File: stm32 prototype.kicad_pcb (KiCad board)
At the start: 4 copper layers, 112 parts, among them J1 USB_B_Mini, J2 Conn_01x06, J3 Conn_02x08_Top_Bottom, J4 Conn_01x10, J5 Conn_02x04_Top_Bottom, Q1 Q_NMOS_GSD, Q10 2N2219, Q11 Q_NMOS_GSD, Q2 Q_NMOS_GSD, Q3 Q_NMOS_GSD, Q4 Q_NMOS_GSD, Q5 Q_NMOS_GSD, Q6 Q_NMOS_GSD, Q7 Q_NMOS_GSD, Q8 Q_NMOS_GSD, Q9 2N2219, SW1 SW_Push, SW2 SW_Push, U1 FT232RL, U2 W25Q128JV-DTR, U3 STM32F407VGTx, U4 LD1117S33TR, U5 ESP32-WROOM, U7 TPS62203DBVR, Y1 Crystal_GND24

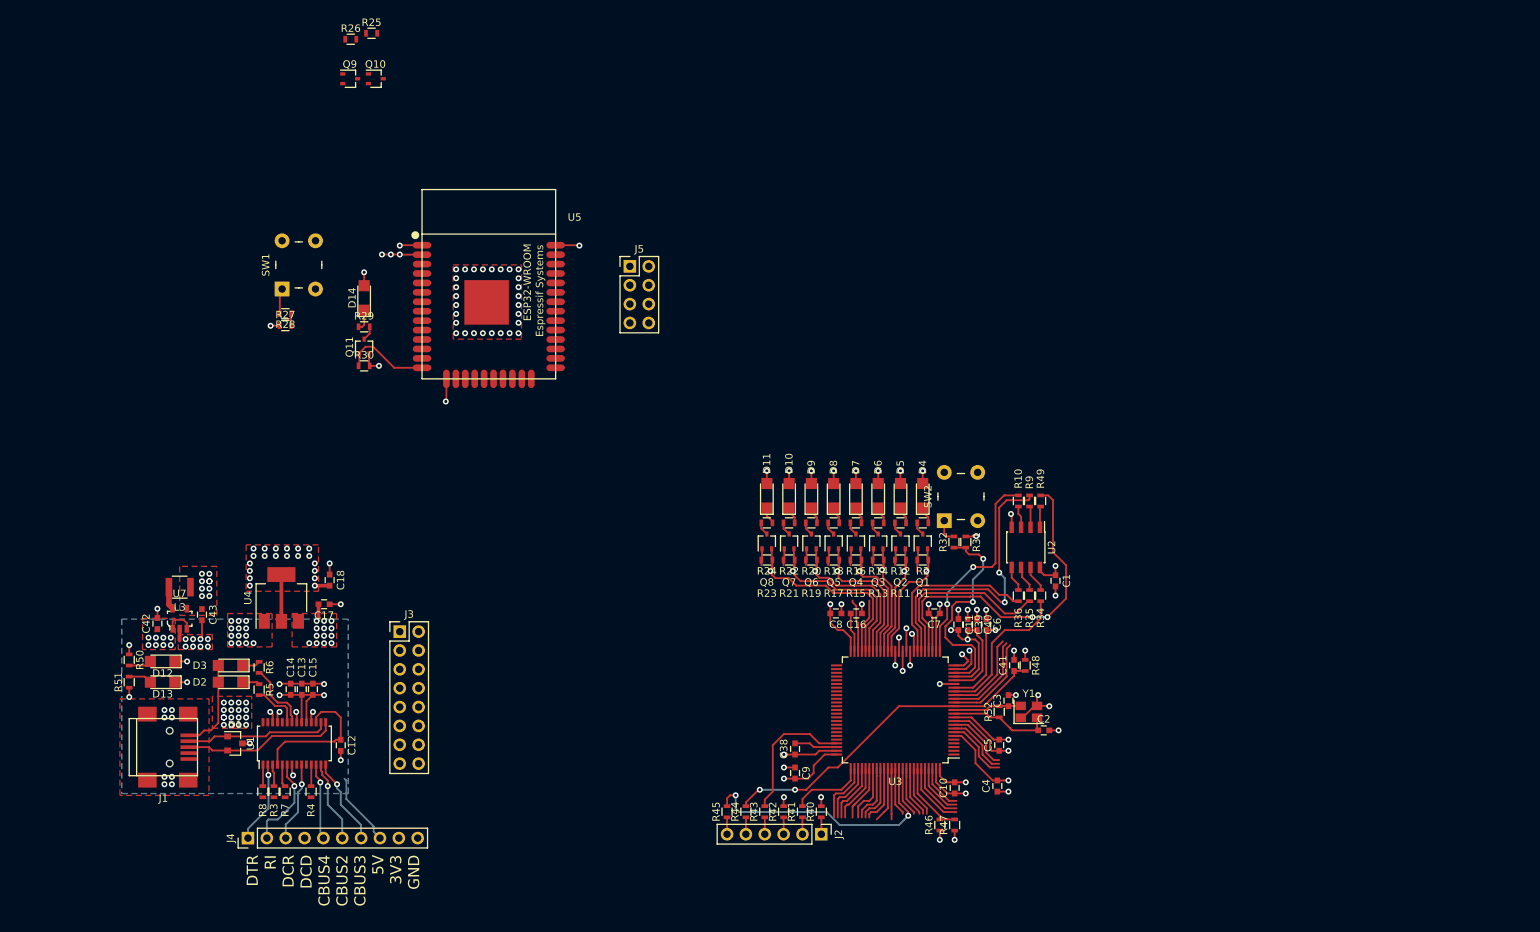
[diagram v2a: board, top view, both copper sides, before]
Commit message: worked on layout, created board outline, started working on fitting the input, esp32, and stm32 sections together
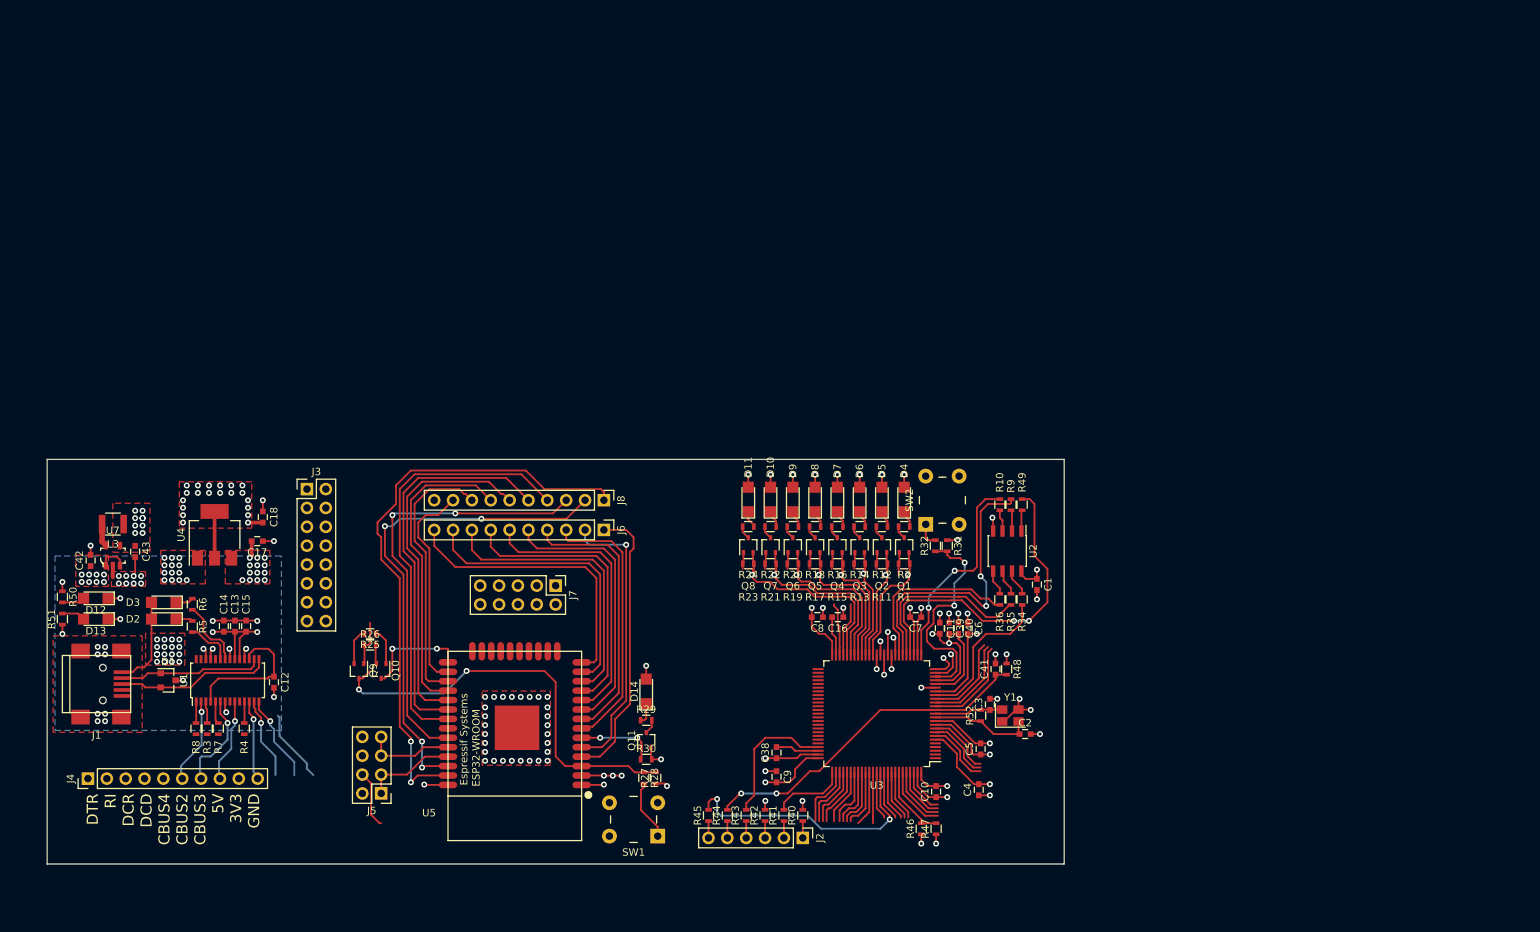
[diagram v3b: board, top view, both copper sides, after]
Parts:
- added J6: Conn_01x10, Pin_Headers:Pin_Header_Straight_1x10_Pitch2.54mm, F.Cu at (137.5, 97.5)
- added J7: Conn_02x05_Top_Bottom, Pin_Headers:Pin_Header_Straight_2x05_Pitch2.54mm, F.Cu at (131.0, 105.0)
- added J8: Conn_01x10, Pin_Headers:Pin_Header_Straight_1x10_Pitch2.54mm, F.Cu at (137.5, 93.5)
- J5: value Conn_02x04_Top_Bottom -> Conn_02x04_Odd_Even
- moved SW1 87.3 mm to (141.5, 136.5), turned to 180 degrees
- moved R26 81.6 mm to (106.0, 113.0)
- moved R25 80.9 mm to (106.0, 111.5), turned to 180 degrees
- moved Q9 79.8 mm to (104.5, 116.5), turned to 270 degrees
- moved Q10 79.8 mm to (107.5, 116.5), turned to 270 degrees
- moved R28 79.0 mm to (142.9, 130.9), turned to 270 degrees
- moved R27 78.7 mm to (144.5, 130.9), turned to 90 degrees
- moved J5 78.5 mm to (107.5, 133.0), turned to 180 degrees
- moved D14 65.2 mm to (143.2, 119.2)
- moved Q11 65.2 mm to (143.2, 125.8)
- moved R29 65.2 mm to (143.2, 123.1)
- moved R30 65.2 mm to (143.2, 128.4)
- moved U5 62.3 mm to (125.5, 126.6), turned to 0 degrees
- moved J4 23.0 mm to (68.0, 131.0)
- moved J3 22.9 mm to (97.5, 92.0)
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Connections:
- J5 pad 2: Net-(J5-Pad1) -> FTDI_ES_RXD
- J5 pad 3: Net-(J5-Pad3) -> Net-(J5-Pad1)
- J5 pad 4: Net-(J5-Pad3) -> ST_ESP_RXD
- J5 pad 5: FTDI_ES_RXD -> Net-(J5-Pad5)
- J5 pad 6: ST_ESP_RXD -> FTDI_ES_TXD
- J5 pad 7: FTDI_ES_TXD -> Net-(J5-Pad5)
- U5 pad 10: (no net) -> Net-(J6-Pad6)
- U5 pad 11: (no net) -> Net-(J6-Pad7)
- U5 pad 12: (no net) -> Net-(J6-Pad8)
- U5 pad 13: (no net) -> Net-(J6-Pad9)
- U5 pad 14: Net-(Q11-Pad1) -> Net-(J6-Pad10)
- U5 pad 15: GND -> Net-(J7-Pad6)
- U5 pad 16: (no net) -> Net-(J7-Pad7)
- U5 pad 17: (no net) -> Net-(J7-Pad8)
- U5 pad 18: (no net) -> Net-(J7-Pad9)
- U5 pad 19: (no net) -> Net-(J7-Pad10)
- U5 pad 20: (no net) -> Net-(J7-Pad5)
- U5 pad 21: (no net) -> Net-(J7-Pad4)
- U5 pad 22: (no net) -> Net-(J7-Pad3)
- U5 pad 23: (no net) -> Net-(J7-Pad2)
- U5 pad 24: (no net) -> Net-(J7-Pad1)
- U5 pad 26: (no net) -> Net-(J8-Pad9)
- U5 pad 27: (no net) -> Net-(J8-Pad8)
- U5 pad 28: (no net) -> Net-(J8-Pad7)
- U5 pad 29: (no net) -> Net-(J8-Pad6)
- U5 pad 30: (no net) -> Net-(J8-Pad5)
- U5 pad 31: (no net) -> Net-(J8-Pad4)
- U5 pad 33: (no net) -> Net-(J8-Pad3)
- U5 pad 34: Net-(J5-Pad3) -> Net-(J5-Pad5)
- U5 pad 36: (no net) -> Net-(J8-Pad2)
- U5 pad 37: (no net) -> Net-(J8-Pad1)
- U5 pad 4: (no net) -> Net-(J6-Pad1)
- U5 pad 5: (no net) -> Net-(J6-Pad2)
- U5 pad 6: (no net) -> Net-(Q11-Pad1)
- U5 pad 7: (no net) -> Net-(J6-Pad3)
- U5 pad 8: (no net) -> Net-(J6-Pad4)
- U5 pad 9: (no net) -> Net-(J6-Pad5)
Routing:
- net Net-(J8-Pad1): track 0.00 -> 79.4 mm, vias 0 -> 2
- net Net-(J8-Pad2): track 0.00 -> 66.6 mm, vias 0 -> 4
- net Net-(J8-Pad3): track 0.00 -> 58.8 mm, vias 0 -> 2
- net Net-(J8-Pad4): track 0.00 -> 57.9 mm
- net ESP_EN: track 1.60 -> 56.5 mm, vias 0 -> 2
- net Net-(J8-Pad5): track 0.00 -> 52.8 mm
- net Net-(J8-Pad6): track 0.00 -> 47.2 mm
- net Net-(J8-Pad7): track 0.00 -> 41.5 mm
- net Net-(J6-Pad10): track 0.00 -> 38.9 mm
- net Net-(J6-Pad9): track 0.00 -> 38.9 mm
- net Net-(J6-Pad8): track 0.00 -> 38.7 mm
- net Net-(J6-Pad2): track 0.00 -> 38.6 mm, vias 0 -> 1
- net Net-(J6-Pad1): track 0.00 -> 38.3 mm
- net Net-(J6-Pad7): track 0.00 -> 38.1 mm
- net Net-(J6-Pad6): track 0.00 -> 37.6 mm
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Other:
- board outline added: 137 x 54.5 mm

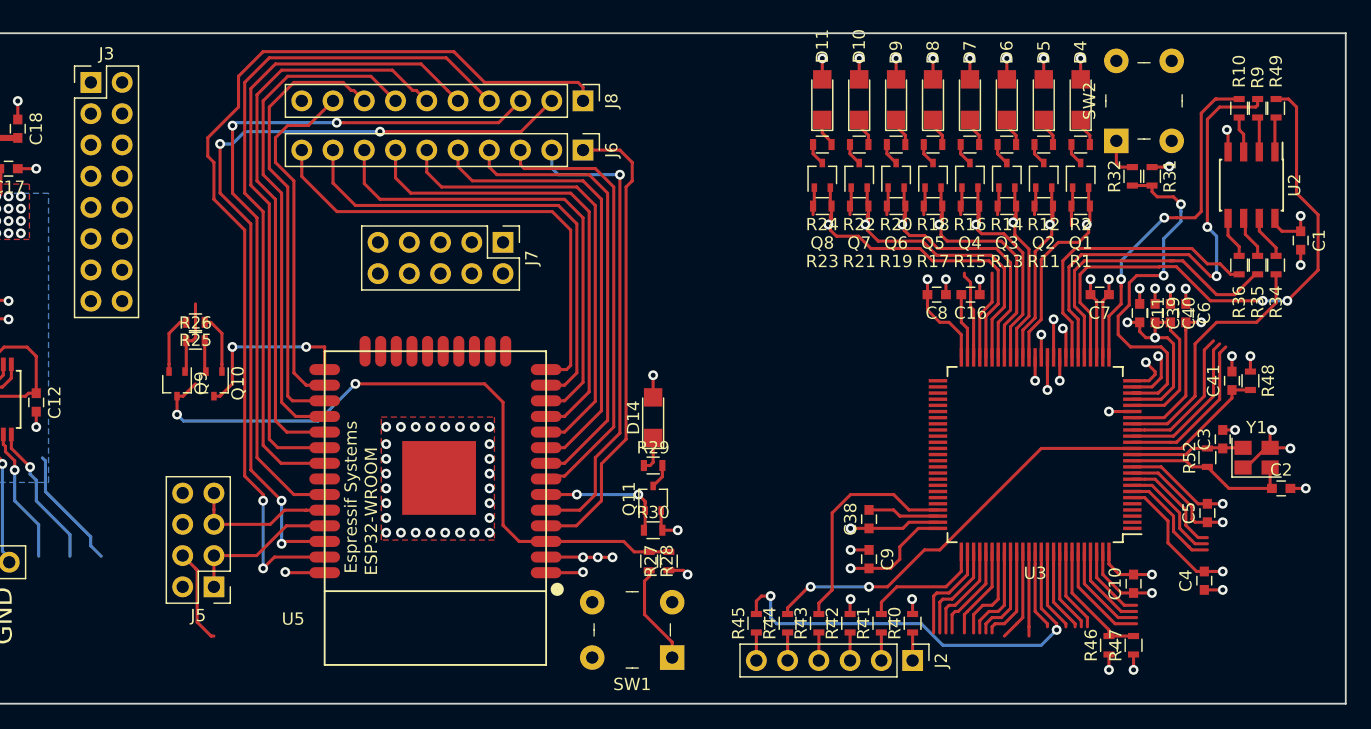
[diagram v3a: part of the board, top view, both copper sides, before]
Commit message: reworked layout of esp32 section
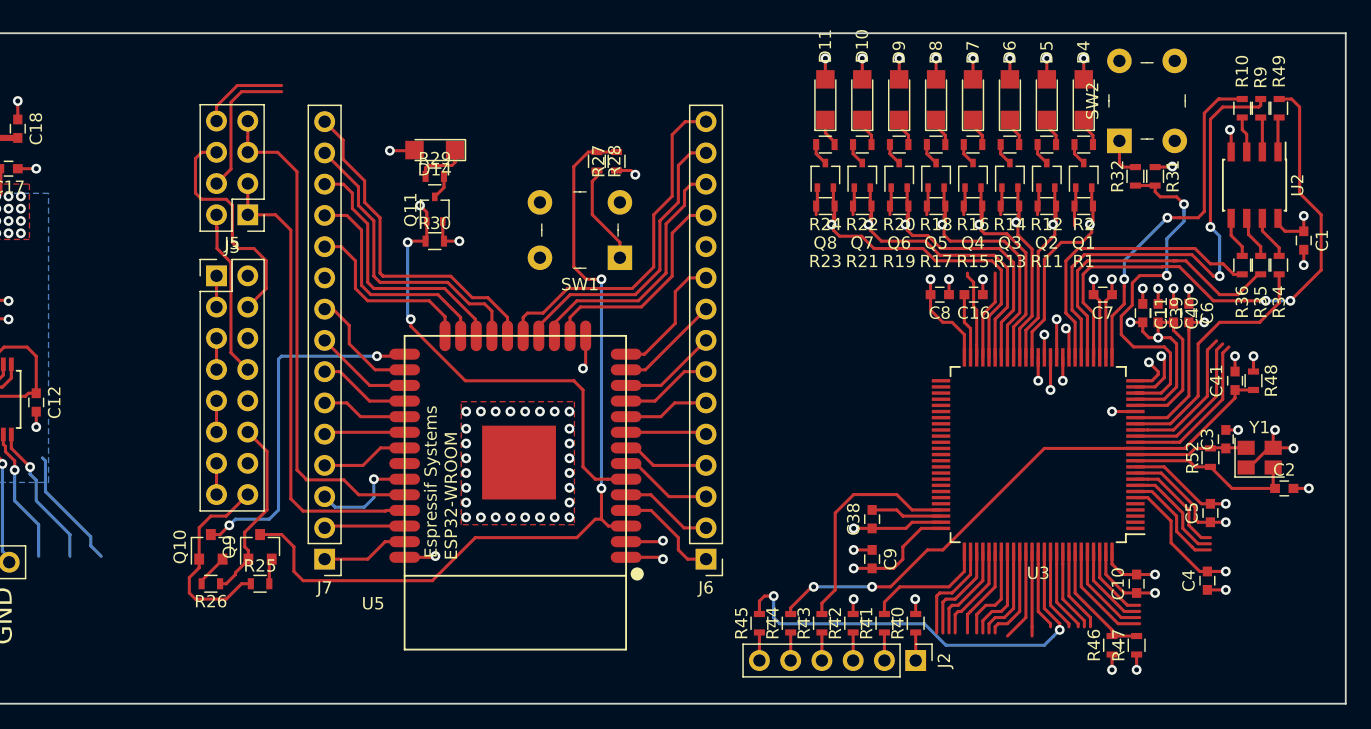
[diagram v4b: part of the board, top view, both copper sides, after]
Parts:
- removed J8: Conn_01x10, Pin_Headers:Pin_Header_Straight_1x10_Pitch2.54mm
- J3: value Conn_02x08_Top_Bottom -> Conn_02x08_Odd_Even
- J6: value Conn_01x10 -> Conn_01x15; footprint Pin_Headers:Pin_Header_Straight_1x10_Pitch2.54mm -> Pin_Headers:Pin_Header_Straight_1x15_Pitch2.54mm
- J7: value Conn_02x05_Top_Bottom -> Conn_01x15; footprint Pin_Headers:Pin_Header_Straight_2x05_Pitch2.54mm -> Pin_Headers:Pin_Header_Straight_1x15_Pitch2.54mm
- Q10, Q9: footprint TO_SOT_Packages_SMD:SOT-323_SC-70 -> TO_SOT_Packages_SMD:SOT-23
- moved J6 34.7 mm to (147.5, 130.8), turned to 180 degrees
- moved R27 32.8 mm to (140.2, 98.4)
- moved R28 32.8 mm to (138.6, 98.4)
- moved SW1 32.8 mm to (137.2, 104.0)
- moved J5 30.4 mm to (110.2, 102.8)
- moved J7 29.6 mm to (116.5, 130.8), turned to 180 degrees
- moved Q11 29.5 mm to (125.5, 102.3)
- moved R29 29.5 mm to (125.5, 99.6)
- moved R30 29.5 mm to (125.5, 104.9)
- moved D14 28.1 mm to (125.5, 97.5), turned to 180 degrees
- moved R25 21.9 mm to (111.2, 132.8), turned to 0 degrees
- moved R26 19.8 mm to (107.2, 132.8), turned to 180 degrees
- moved J3 18.7 mm to (107.7, 107.7)
- moved Q9 14.9 mm to (111.2, 129.8), turned to 90 degrees
- moved Q10 13.3 mm to (107.2, 129.8), turned to 90 degrees
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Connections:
- net Net-(J6-Pad1) renamed SENSOR_VP
- net Net-(J6-Pad10) renamed IO12
- net Net-(J6-Pad2) renamed SENSOR_VN
- net Net-(J6-Pad3) renamed IO35
- net Net-(J6-Pad4) renamed IO32
- net Net-(J6-Pad5) renamed IO33
- net Net-(J6-Pad6) renamed IO25
- net Net-(J6-Pad7) renamed IO26
- net Net-(J6-Pad8) renamed IO27
- net Net-(J6-Pad9) renamed IO14
- J3 pad 10: FTDI_ES_TXD -> FTDI_ST_RTS
- J3 pad 11: FTDI_ST_RXD -> Net-(J3-Pad11)
- J3 pad 12: FTDI_ES_RXD -> FTDI_ES_RTS
- J3 pad 13: FTDI_ST_RTS -> Net-(J3-Pad13)
- J3 pad 14: FTDI_ES_RTS -> (no net)
- J3 pad 15: (no net) -> Net-(J3-Pad13)
- J3 pad 2: Net-(J3-Pad1) -> FTDI_ST_TXD
- J3 pad 3: Net-(J3-Pad3) -> Net-(J3-Pad1)
- J3 pad 4: Net-(J3-Pad3) -> FTDI_ES_TXD
- J3 pad 6: Net-(J3-Pad5) -> FTDI_ST_RXD
- J3 pad 7: Net-(J3-Pad7) -> Net-(J3-Pad5)
- J3 pad 8: Net-(J3-Pad7) -> FTDI_ES_RXD
- J3 pad 9: FTDI_ST_TXD -> Net-(J3-Pad11)
- J4 pad 1: Net-(J3-Pad7) -> Net-(J3-Pad13)
- J7 pad 1: Net-(J7-Pad1) -> IO23
- J7 pad 10: Net-(J7-Pad10) -> +3V3
- J7 pad 2: Net-(J7-Pad2) -> IO22
- J7 pad 3: Net-(J7-Pad3) -> IO21
- J7 pad 4: Net-(J7-Pad4) -> IO19
- J7 pad 5: Net-(J7-Pad5) -> IO18
- J7 pad 6: Net-(J7-Pad6) -> IO5
- J7 pad 7: Net-(J7-Pad7) -> IO17
- J7 pad 8: Net-(J7-Pad8) -> IO16
- J7 pad 9: Net-(J7-Pad9) -> IO4
- R3 pad 1: Net-(J3-Pad5) -> Net-(J3-Pad11)
- U1 pad 2: Net-(J3-Pad7) -> Net-(J3-Pad13)
- U1 pad 5: Net-(J3-Pad3) -> Net-(J3-Pad5)
- U5 pad 15: Net-(J7-Pad6) -> GND
- U5 pad 16: Net-(J7-Pad7) -> IO13
- U5 pad 17: Net-(J7-Pad8) -> SD2
- U5 pad 18: Net-(J7-Pad9) -> SD3
- U5 pad 19: Net-(J7-Pad10) -> CMD
- U5 pad 20: Net-(J7-Pad5) -> CLK
- U5 pad 21: Net-(J7-Pad4) -> SD0
- U5 pad 22: Net-(J7-Pad3) -> SD1
- U5 pad 23: Net-(J7-Pad2) -> IO15
- U5 pad 24: Net-(J7-Pad1) -> IO2
- U5 pad 26: Net-(J8-Pad9) -> IO4
- U5 pad 27: Net-(J8-Pad8) -> IO16
- U5 pad 28: Net-(J8-Pad7) -> IO17
- U5 pad 29: Net-(J8-Pad6) -> IO5
- U5 pad 30: Net-(J8-Pad5) -> IO18
- U5 pad 31: Net-(J8-Pad4) -> IO19
- U5 pad 33: Net-(J8-Pad3) -> IO21
- U5 pad 36: Net-(J8-Pad2) -> IO22
- U5 pad 37: Net-(J8-Pad1) -> IO23
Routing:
- net Net-(J8-Pad1): track 79.4 -> 0.00 mm, vias 2 -> 0
- net Net-(J8-Pad2): track 66.6 -> 0.00 mm, vias 4 -> 0
- net Net-(J8-Pad3): track 58.8 -> 0.00 mm, vias 2 -> 0
- net Net-(J8-Pad4): track 57.9 -> 0.00 mm
- net Net-(J8-Pad5): track 52.8 -> 0.00 mm
- net Net-(J8-Pad6): track 47.2 -> 0.00 mm
- net Net-(J8-Pad7): track 41.5 -> 0.00 mm
- net Net-(J8-Pad8): track 36.4 -> 0.00 mm
- net SENSOR_VN: track 38.6 -> 7.61 mm, vias 1 -> 0
- net IO27: track 38.7 -> 8.02 mm
- net IO26: track 38.1 -> 7.49 mm
- net IO25: track 37.6 -> 6.96 mm
- net IO33: track 37.0 -> 6.56 mm
- net IO14: track 38.9 -> 8.54 mm
- net IO32: track 36.8 -> 7.09 mm
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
